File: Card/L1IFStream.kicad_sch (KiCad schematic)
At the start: 107 parts, among them J1 Conn_Coaxial, J2 USB_A, J3 RF_Shield_One_Piece, J4 Conn_Coaxial, U1 MAX2769ETI+T, U10 74LVC374, U11 74HC2GU04, U2 TPS717285DCKR, U3 TPS717285DCKR, U4 NCP164CSN330T1G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

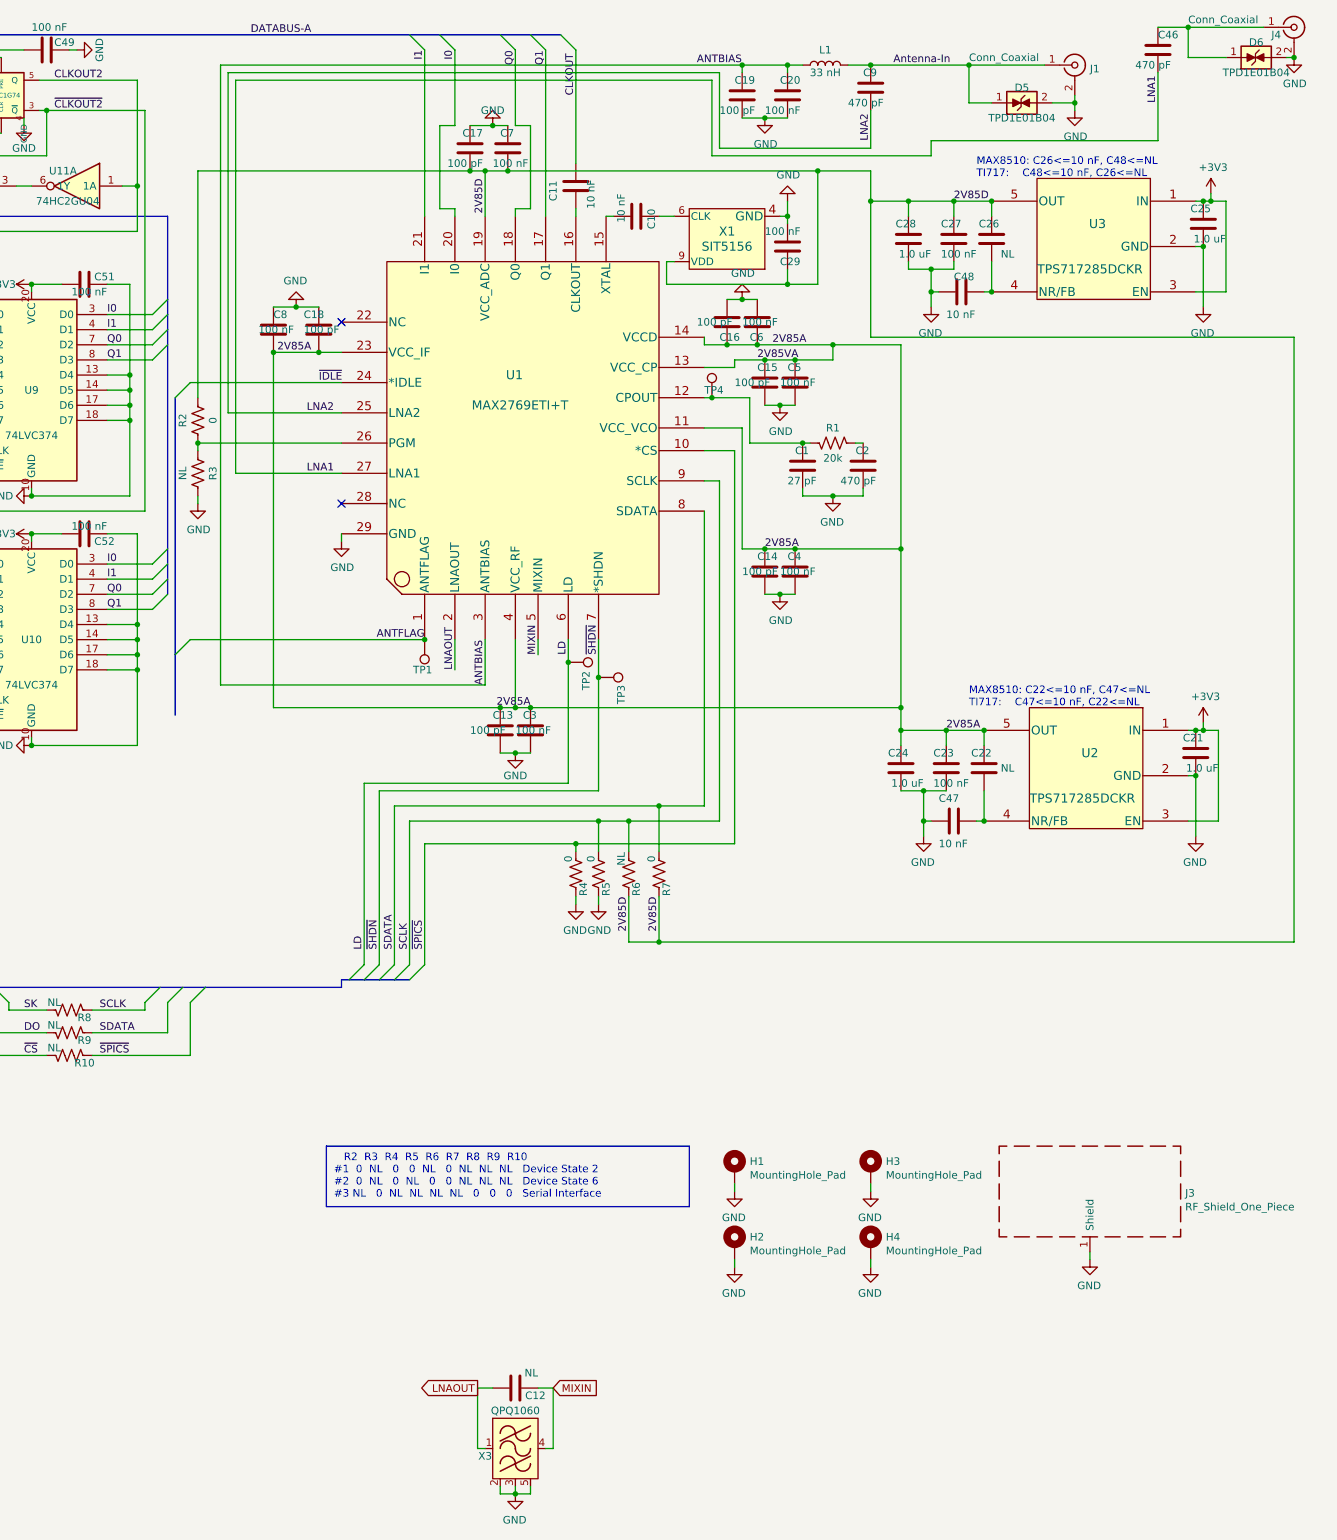
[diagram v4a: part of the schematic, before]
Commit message: Reoriented schematic
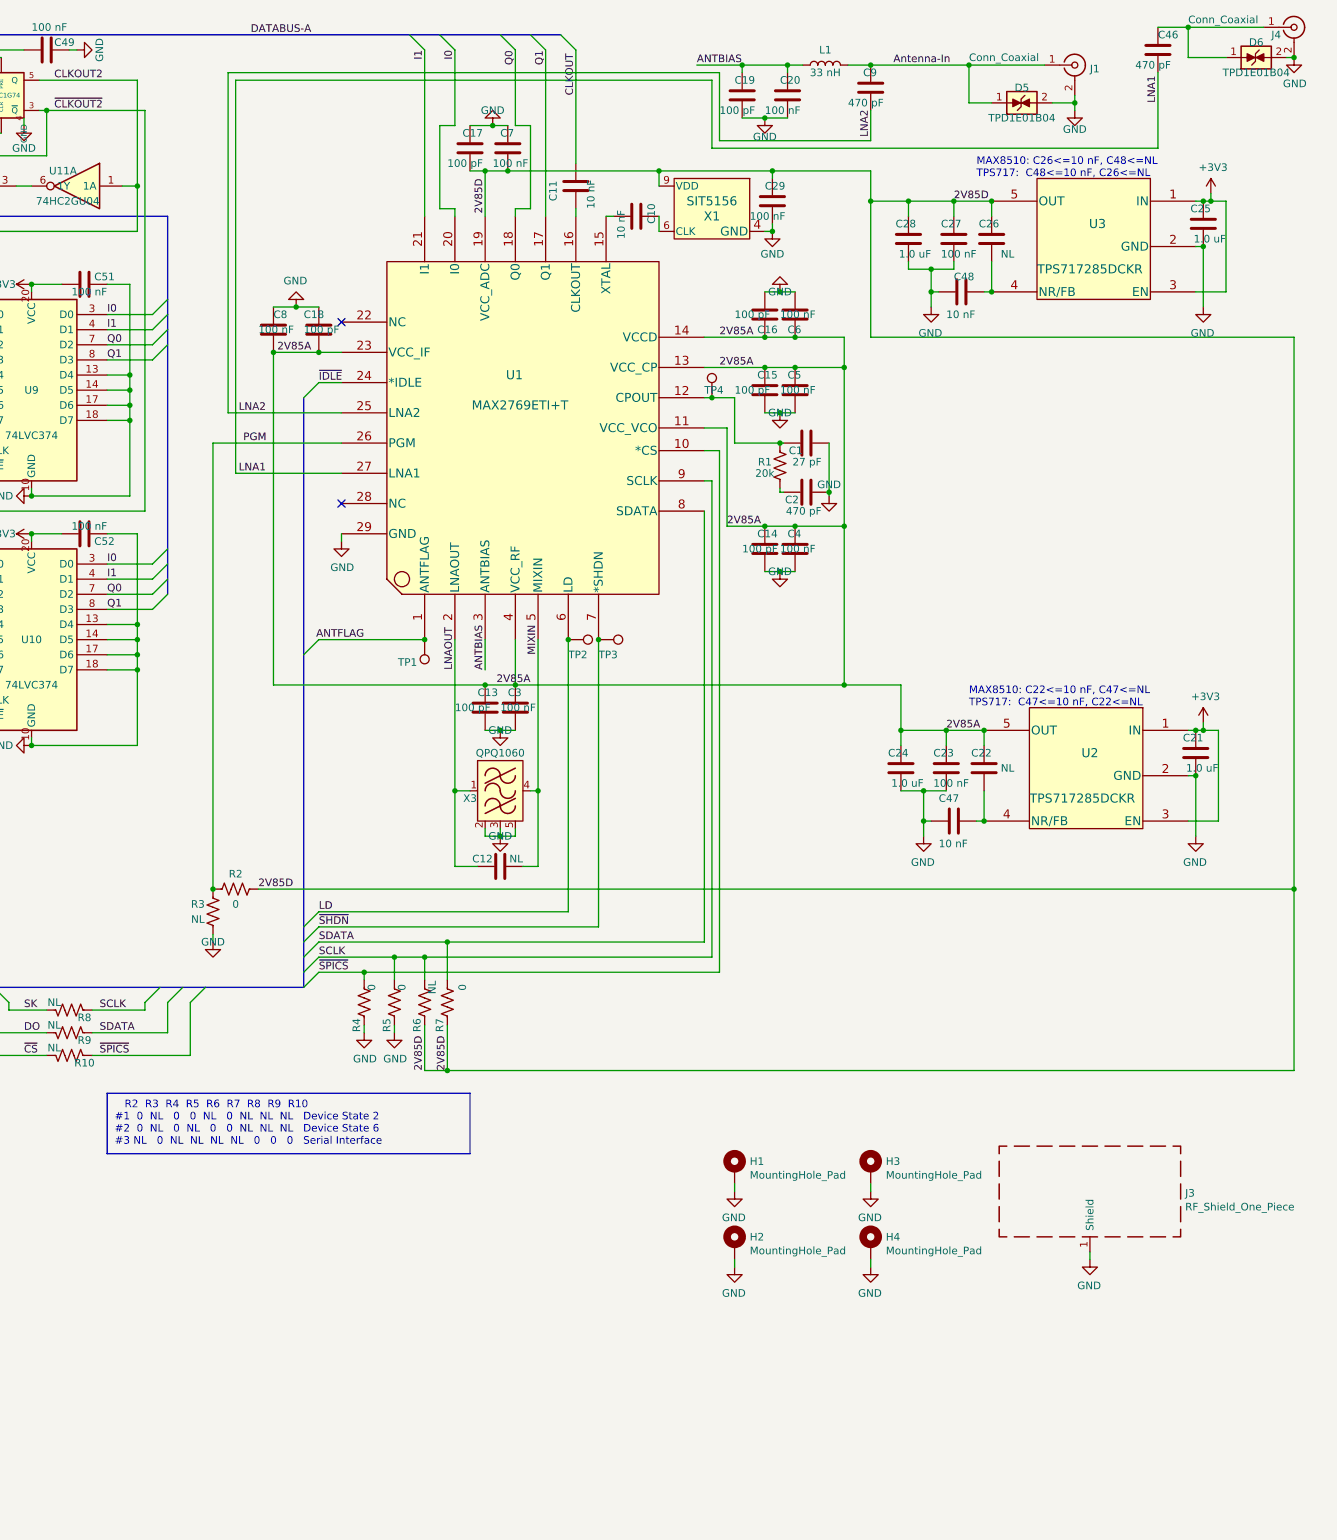
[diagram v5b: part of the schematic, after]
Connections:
- net ANTBIAS: no longer U1.17 (Q1), U1.18 (Q0), U10.7 (D2), U10.8 (D3), U9.7 (D2), U9.8 (D3)
- net PGM: now reaches R2.2, R3.2, U1.26 (PGM)
- new net Q0: U1.18 (Q0), U10.7 (D2), U9.7 (D2)
- new net Q1: U1.17 (Q1), U10.8 (D3), U9.8 (D3)
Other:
- note added: "MAX8510: C22<=10 nF, C47<=NL TPS717: C47<=10 nF, C22<=NL"
- note added: "MAX8510: C26<=10 nF, C48<=NL TPS717: C48<=10 nF, C26<=NL"
- note removed: "MAX8510: C22<=10 nF, C47<=NL TI717: C47<=10 nF, C22<=NL"
- note removed: "MAX8510: C26<=10 nF, C48<=NL TI717: C48<=10 nF, C26<=NL"
- moved on the sheet: C12, C13, C14, C15, C16, C3, C4, C5, C6, R4, R5, R6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

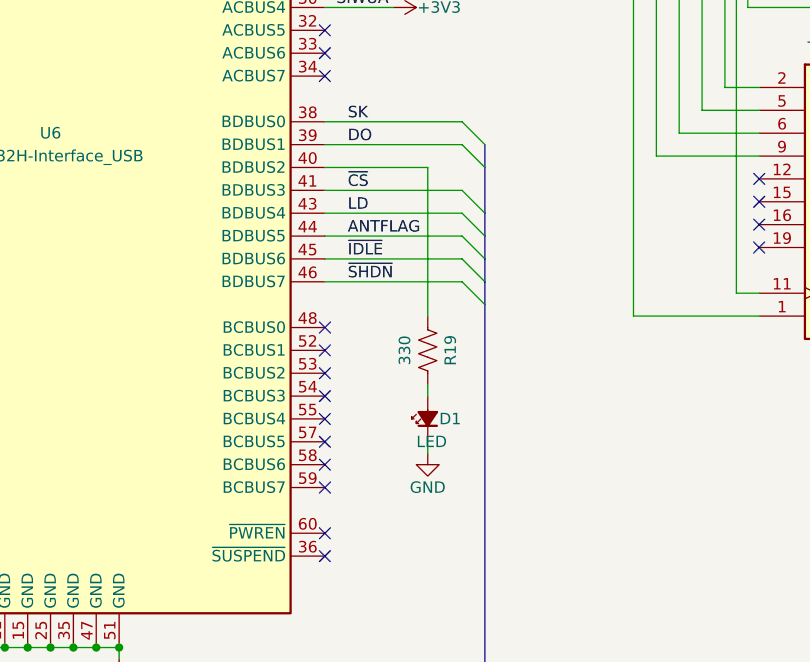
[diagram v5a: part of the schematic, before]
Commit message: Fixed LED Circuit
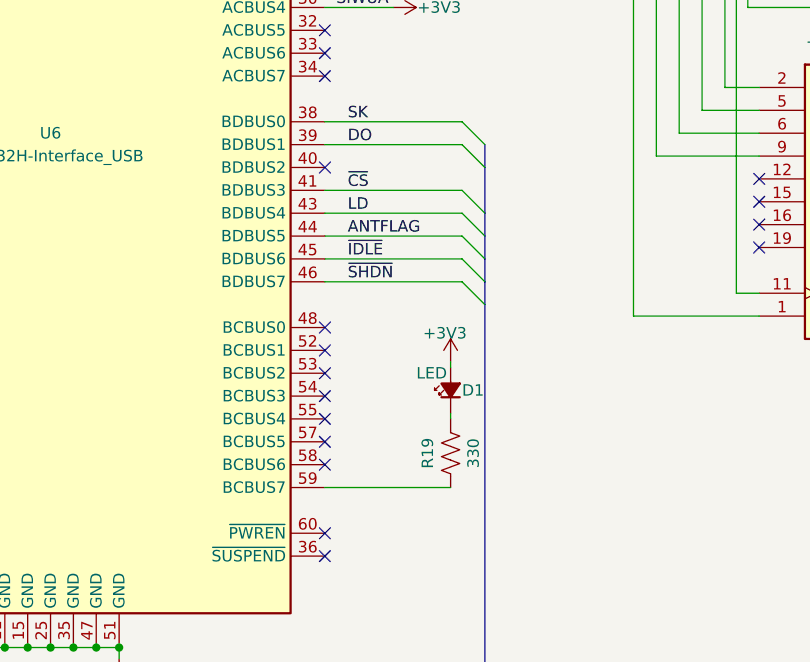
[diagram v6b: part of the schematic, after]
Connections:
- net +3V3: now also D1.2 (A)
- net GND: no longer D1.1 (K)
- net at U6.40 (BDBUS2): no longer R19.2
- net at U6.59 (BCBUS7): now also R19.2
- net at R19.1: now also D1.1 (K); no longer D1.2 (A)
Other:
- moved on the sheet: R19
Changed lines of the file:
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@@
   (no_connect (at 193.04 80.01))
   (no_connect (at 144.78 135.89))
-  (no_connect (at 144.78 148.59))
   (no_connect (at 144.78 143.51))
   (no_connect (at 144.78 138.43))
   (no_connect (at 144.78 153.67))
   (no_connect (at 144.78 146.05))
+  (no_connect (at 144.78 113.03))
   (no_connect (at 193.04 72.39))
   (no_connect (at 144.78 100.33))
@@
     (stroke (width 0) (type default))
   )
+  (wire (pts (xy 158.75 134.62) (xy 158.75 135.255))
+    (stroke (width 0) (type default))
+  )
   (wire (pts (xy 254 170.18) (xy 266.7 170.18))
     (stroke (width 0) (type default))
@@
     (stroke (width 0) (type default))
   )
-  (wire (pts (xy 144.78 113.03) (xy 156.21 113.03))
-    (stroke (width 0) (type default))
-  )
   (wire (pts (xy 223.52 22.86) (xy 223.52 40.64))
     (stroke (width 0) (type default))
@@
     (stroke (width 0) (type default))
   )
-  (wire (pts (xy 156.21 113.03) (xy 156.21 129.54))
-    (stroke (width 0) (type default))
-  )
   (wire (pts (xy 232.41 177.8) (xy 232.41 186.69))
     (stroke (width 0) (type default))
@@
     (stroke (width 0) (type default))
   )
-  (wire (pts (xy 156.21 137.16) (xy 156.21 138.43))
-    (stroke (width 0) (type default))
-  )
   (bus (pts (xy 274.32 15.24) (xy 284.48 15.24))
     (stroke (width 0) (type default))
@@
     (stroke (width 0) (type default))
   )
+  (wire (pts (xy 144.78 148.59) (xy 158.75 148.59))
+    (stroke (width 0) (type default))
+  )
   (wire (pts (xy 20.32 100.33) (xy 21.59 100.33))
     (stroke (width 0) (type default))
@@
     (stroke (width 0) (type default))
   )
+  (wire (pts (xy 158.75 140.335) (xy 158.75 140.97))
+    (stroke (width 0) (type default))
+  )
   (wire (pts (xy 223.52 116.84) (xy 223.52 119.38))
     (stroke (width 0) (type default))
@@
     (stroke (width 0) (type default))
   )
-  (wire (pts (xy 156.21 143.51) (xy 156.21 144.78))
-    (stroke (width 0) (type default))
-  )
   (wire (pts (xy 360.68 45.72) (xy 360.68 43.18))
     (stroke (width 0) (type default))
@@
     )
   )
-  (symbol (lib_id "L1IFStream-rescue:R_US-MAX2769FT2232H") (at 156.21 133.35 180) (unit 1)
+  (symbol (lib_id "L1IFStream-rescue:R_US-MAX2769FT2232H") (at 158.75 144.78 0) (unit 1)
     (in_bom yes) (on_board yes) (dnp no)
-    (property "Reference" "R19" (at 158.75 133.35 90)
+    (property "Reference" "R19" (at 156.21 144.78 90)
       (effects (font (size 1.27 1.27)))
     )
-    (property "Value" "330" (at 153.67 133.35 90)
+    (property "Value" "330" (at 161.29 144.78 90)
       (effects (font (size 1.27 1.27)))
     )
-    (property "Footprint" "L1IFStream:R_0603_1608Metric" (at 155.194 133.096 90)
+    (property "Footprint" "L1IFStream:R_0603_1608Metric" (at 159.766 145.034 90)
       (effects (font (size 1.27 1.27)) hide)
     )
-    (property "Datasheet" "https://www.koaspeer.com/pdfs/RK73H.pdf" (at 156.21 133.35 0)
+    (property "Datasheet" "https://www.koaspeer.com/pdfs/RK73H.pdf" (at 158.75 144.78 0)
       (effects (font (size 1.27 1.27)) hide)
     )
-    (property "Description" "RES 330 OHM 1% 1/8W 0603" (at 156.21 133.35 90)
+    (property "Description" "RES 330 OHM 1% 1/8W 0603" (at 158.75 144.78 90)
       (effects (font (size 1.27 1.27)) hide)
     )
-    (property "Digi-Key" "2019-RK73H1JTTD3300FDKR-ND" (at 156.21 133.35 90)
+    (property "Digi-Key" "2019-RK73H1JTTD3300FDKR-ND" (at 158.75 144.78 90)
       (effects (font (size 1.27 1.27)) hide)
     )
-    (property "MPN" "RK73H1JTTD3300F" (at 156.21 133.35 90)
+    (property "MPN" "RK73H1JTTD3300F" (at 158.75 144.78 90)
       (effects (font (size 1.27 1.27)) hide)
     )
@@
     )
   )
-  (symbol (lib_id "power:GND") (at 156.21 144.78 0) (unit 1)
-    (in_bom yes) (on_board yes) (dnp no)
-    (property "Reference" "#PWR02" (at 156.21 151.13 0)
-      (effects (font (size 1.27 1.27)) hide)
-    )
-    (property "Value" "GND" (at 156.21 148.59 0)
-      (effects (font (size 1.27 1.27)))
-    )
-    (property "Footprint" "" (at 156.21 144.78 0)
-      (effects (font (size 1.27 1.27)) hide)
-    )
-    (property "Datasheet" "" (at 156.21 144.78 0)
-      (effects (font (size 1.27 1.27)) hide)
-    )
-    (pin "1")
-    (instances
-      (project "L1IFStream"
-        (path "/e22d8814-0b83-456b-8939-db783783fcf1"
-          (reference "#PWR02") (unit 1)
-        )
-      )
-    )
-  )
   (symbol (lib_id "L1IFStream-rescue:R_US-MAX2769FT2232H") (at 236.22 162.56 180) (unit 1)
     (in_bom yes) (on_board yes) (dnp no)
@@
     )
   )
-  (symbol (lib_id "L1IFStream:LED_Small_Filled") (at 156.21 140.97 90) (unit 1)
-    (in_bom yes) (on_board yes) (dnp no)
-    (property "Reference" "D1" (at 157.48 140.97 90)
-      (effects (font (size 1.27 1.27)) (justify right))
-    )
-    (property "Value" "LED" (at 154.94 143.51 90)
-      (effects (font (size 1.27 1.27)) (justify right))
-    )
-    (property "Footprint" "L1IFStream:LED_0603_1608Metric" (at 156.21 140.97 90)
-      (effects (font (size 1.27 1.27)) hide)
-    )
-    (property "Datasheet" "~" (at 156.21 140.97 90)
-      (effects (font (size 1.27 1.27)) hide)
-    )
-    (property "Digi-Key" "QBLP601-AG1-2943" (at 156.21 140.97 90)
-      (effects (font (size 1.27 1.27)) hide)
-    )
-    (property "MPN" "QBLP601-AG1-2943" (at 156.21 140.97 90)
-      (effects (font (size 1.27 1.27)) hide)
-    )
-    (pin "1")
-    (pin "2")
-    (instances
-      (project "L1IFStream"
-        (path "/e22d8814-0b83-456b-8939-db783783fcf1"
-          (reference "D1") (unit 1)
-        )
-      )
-    )
-  )
   (symbol (lib_id "L1IFStream-rescue:R_US-MAX2769FT2232H") (at 331.47 87.63 0) (unit 1)
     (in_bom yes) (on_board yes) (dnp no)
@@
     )
   )
+  (symbol (lib_id "power:+3V3") (at 158.75 134.62 0) (unit 1)
+    (in_bom yes) (on_board yes) (dnp no)
+    (property "Reference" "#PWR02" (at 158.75 138.43 0)
+      (effects (font (size 1.27 1.27)) hide)
+    )
+    (property "Value" "+3V3" (at 158.115 131.445 0)
+      (effects (font (size 1.27 1.27)))
+    )
+    (property "Footprint" "" (at 158.75 134.62 0)
+      (effects (font (size 1.27 1.27)) hide)
+    )
+    (property "Datasheet" "" (at 158.75 134.62 0)
+      (effects (font (size 1.27 1.27)) hide)
+    )
+    (pin "1")
+    (instances
+      (project "L1IFStream"
+        (path "/e22d8814-0b83-456b-8939-db783783fcf1"
+          (reference "#PWR02") (unit 1)
+        )
+      )
+    )
+  )
   (symbol (lib_id "L1IFStream:74LVC1G04") (at 176.53 27.94 0) (unit 1)
     (in_bom yes) (on_board yes) (dnp no)
@@
         )
       )
+    )
+  )
+  (symbol (lib_id "L1IFStream:LED_Small_Filled") (at 158.75 137.795 90) (unit 1)
+    (in_bom yes) (on_board yes) (dnp no)
+    (property "Reference" "D1" (at 160.02 137.795 90)
+      (effects (font (size 1.27 1.27)) (justify right))
+    )
+    (property "Value" "LED" (at 154.94 135.89 90)
+      (effects (font (size 1.27 1.27)) (justify right))
+    )
+    (property "Footprint" "L1IFStream:LED_0603_1608Metric" (at 158.75 137.795 90)
+      (effects (font (size 1.27 1.27)) hide)
+    )
+    (property "Datasheet" "~" (at 158.75 137.795 90)
+      (effects (font (size 1.27 1.27)) hide)
+    )
+    (property "Digi-Key" "QBLP601-AG1-2943" (at 158.75 137.795 90)
+      (effects (font (size 1.27 1.27)) hide)
+    )
+    (property "MPN" "QBLP601-AG1-2943" (at 158.75 137.795 90)
+      (effects (font (size 1.27 1.27)) hide)
+    )
+    (pin "1")
+    (pin "2")
+    (instances
+      (project "L1IFStream"
+        (path "/e22d8814-0b83-456b-8939-db783783fcf1"
+          (reference "D1") (unit 1)
+        )
+      )
